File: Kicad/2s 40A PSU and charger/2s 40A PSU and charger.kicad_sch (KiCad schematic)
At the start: 0 parts

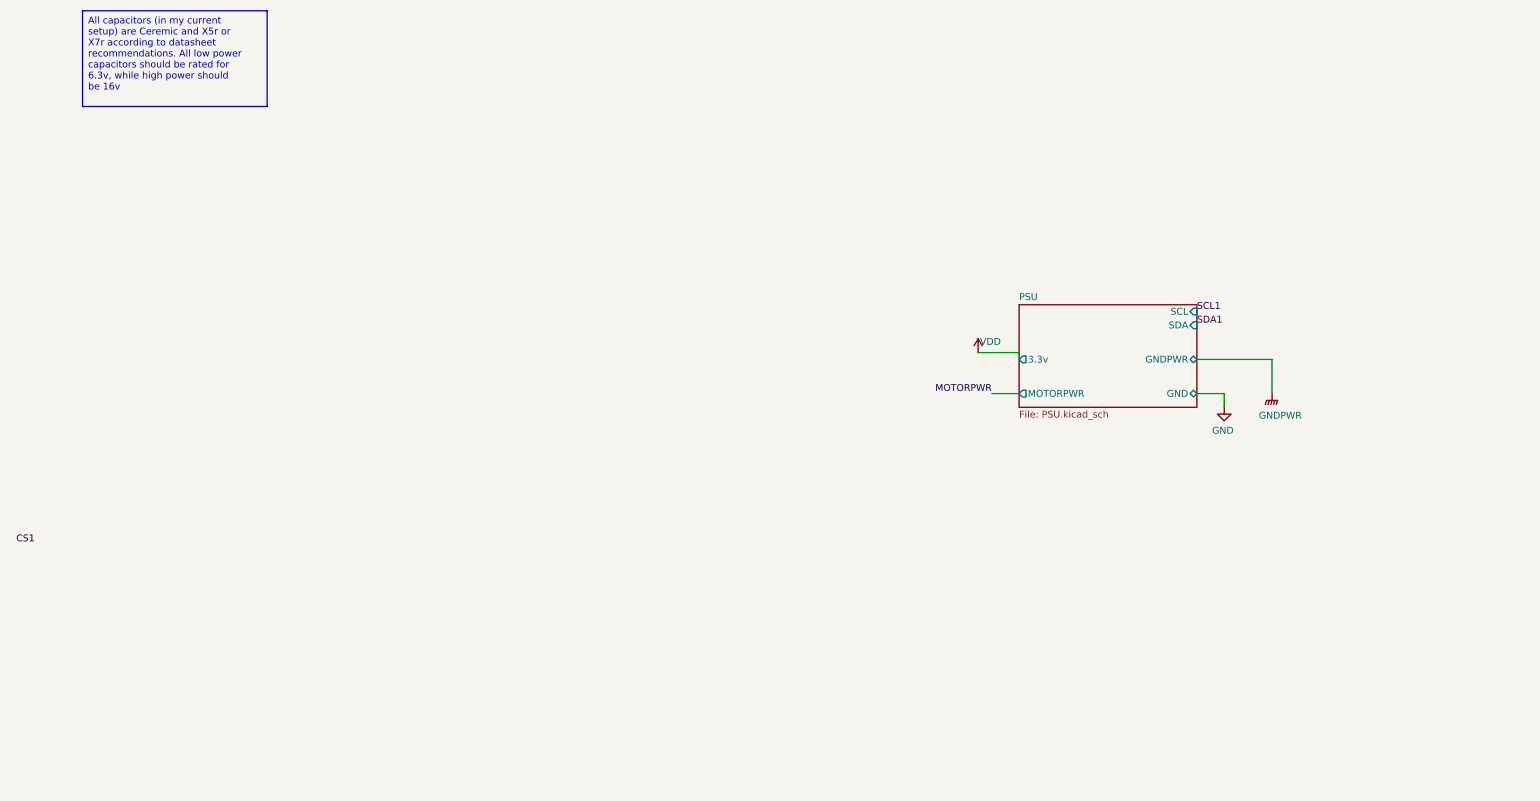
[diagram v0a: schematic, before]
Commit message: Rearranged schematic hierarchy
It should be clearer than the original design from my testing board. I haven't changed any of the design things except getting the correct small transistor footprint (errata from before)
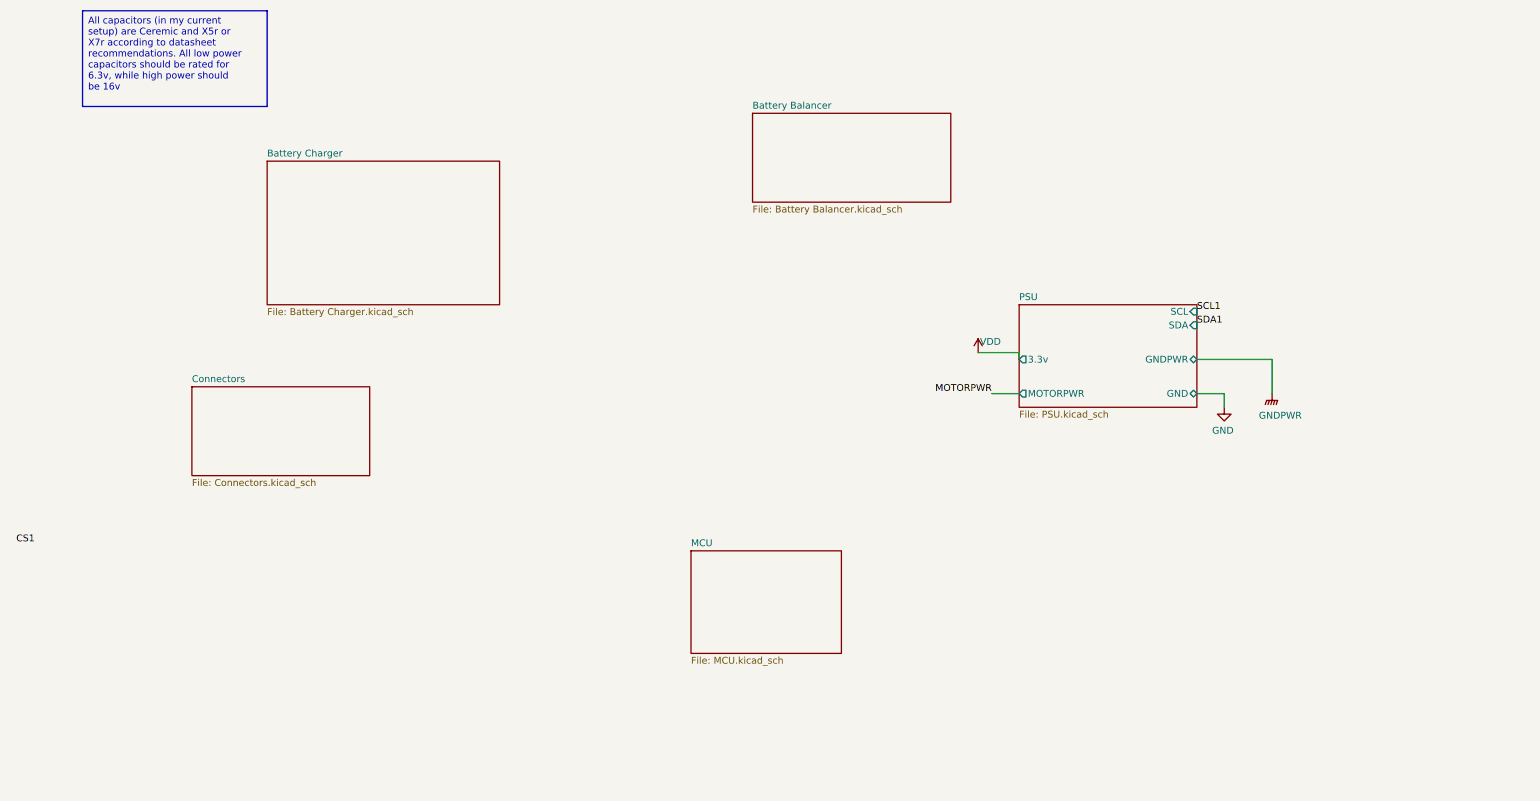
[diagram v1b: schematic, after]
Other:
- added sheet Battery Balancer (Battery Balancer.kicad_sch)
- added sheet Battery Charger (Battery Charger.kicad_sch)
- added sheet Connectors (Connectors.kicad_sch)
- added sheet MCU (MCU.kicad_sch)
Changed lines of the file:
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@@
+	)
+	(sheet
+		(at 40.64 83.82)
+		(size 33.02 16.51)
+		(fields_autoplaced yes)
+		(stroke
+			(width 0.1524)
+			(type solid)
+		)
+		(fill
+			(color 0 0 0 0.0000)
+		)
+		(property "Sheetname" "Connectors"
+			(at 40.64 83.1084 0)
+			(effects
+				(font
+					(size 1.27 1.27)
+				)
+				(justify left bottom)
+			)
+		)
+		(property "Sheetfile" "Connectors.kicad_sch"
+			(at 40.64 100.9146 0)
+			(effects
+				(font
+					(size 1.27 1.27)
+				)
+				(justify left top)
+			)
+		)
+		(instances
+			(project "2s 40A PSU and charger"
+				(path "/eb3f183d-8bb1-43a5-a363-092ed67891e3"
+					(page "5")
+				)
+			)
+		)
+	)
+	(sheet
+		(at 54.61 41.91)
+		(size 43.18 26.67)
+		(fields_autoplaced yes)
+		(stroke
+			(width 0.1524)
+			(type solid)
+		)
+		(fill
+			(color 0 0 0 0.0000)
+		)
+		(property "Sheetname" "Battery Charger"
+			(at 54.61 41.1984 0)
+			(effects
+				(font
+					(size 1.27 1.27)
+				)
+				(justify left bottom)
+			)
+		)
+		(property "Sheetfile" "Battery Charger.kicad_sch"
+			(at 54.61 69.1646 0)
+			(effects
+				(font
+					(size 1.27 1.27)
+				)
+				(justify left top)
+			)
+		)
+		(instances
+			(project "2s 40A PSU and charger"
+				(path "/eb3f183d-8bb1-43a5-a363-092ed67891e3"
+					(page "3")
+				)
+			)
+		)
+	)
+	(sheet
+		(at 133.35 114.3)
+		(size 27.94 19.05)
+		(fields_autoplaced yes)
+		(stroke
+			(width 0.1524)
+			(type solid)
+		)
+		(fill
+			(color 0 0 0 0.0000)
+		)
+		(property "Sheetname" "MCU"
+			(at 133.35 113.5884 0)
+			(effects
+				(font
+					(size 1.27 1.27)
+				)
+				(justify left bottom)
+			)
+		)
+		(property "Sheetfile" "MCU.kicad_sch"
+			(at 133.35 133.9346 0)
+			(effects
+				(font
+					(size 1.27 1.27)
+				)
+				(justify left top)
+			)
+		)
+		(instances
+			(project "2s 40A PSU and charger"
+				(path "/eb3f183d-8bb1-43a5-a363-092ed67891e3"
+					(page "6")
+				)
+			)
+		)
+	)
+	(sheet
+		(at 144.78 33.02)
+		(size 36.83 16.51)
+		(fields_autoplaced yes)
+		(stroke
+			(width 0.1524)
+			(type solid)
+		)
+		(fill
+			(color 0 0 0 0.0000)
+		)
+		(property "Sheetname" "Battery Balancer"
+			(at 144.78 32.3084 0)
+			(effects
+				(font
+					(size 1.27 1.27)
+				)
+				(justify left bottom)
+			)
+		)
+		(property "Sheetfile" "Battery Balancer.kicad_sch"
+			(at 144.78 50.1146 0)
+			(effects
+				(font
+					(size 1.27 1.27)
+				)
+				(justify left top)
+			)
+		)
+		(instances
+			(project "2s 40A PSU and charger"
+				(path "/eb3f183d-8bb1-43a5-a363-092ed67891e3"
+					(page "4")
+				)
+			)
+		)
 	)
 	(sheet

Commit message: Reworked PSU to use CH32X035 and USB-PD
This will save a few bucks and will actually be a cooler solution than just a DC jack connected to some pads
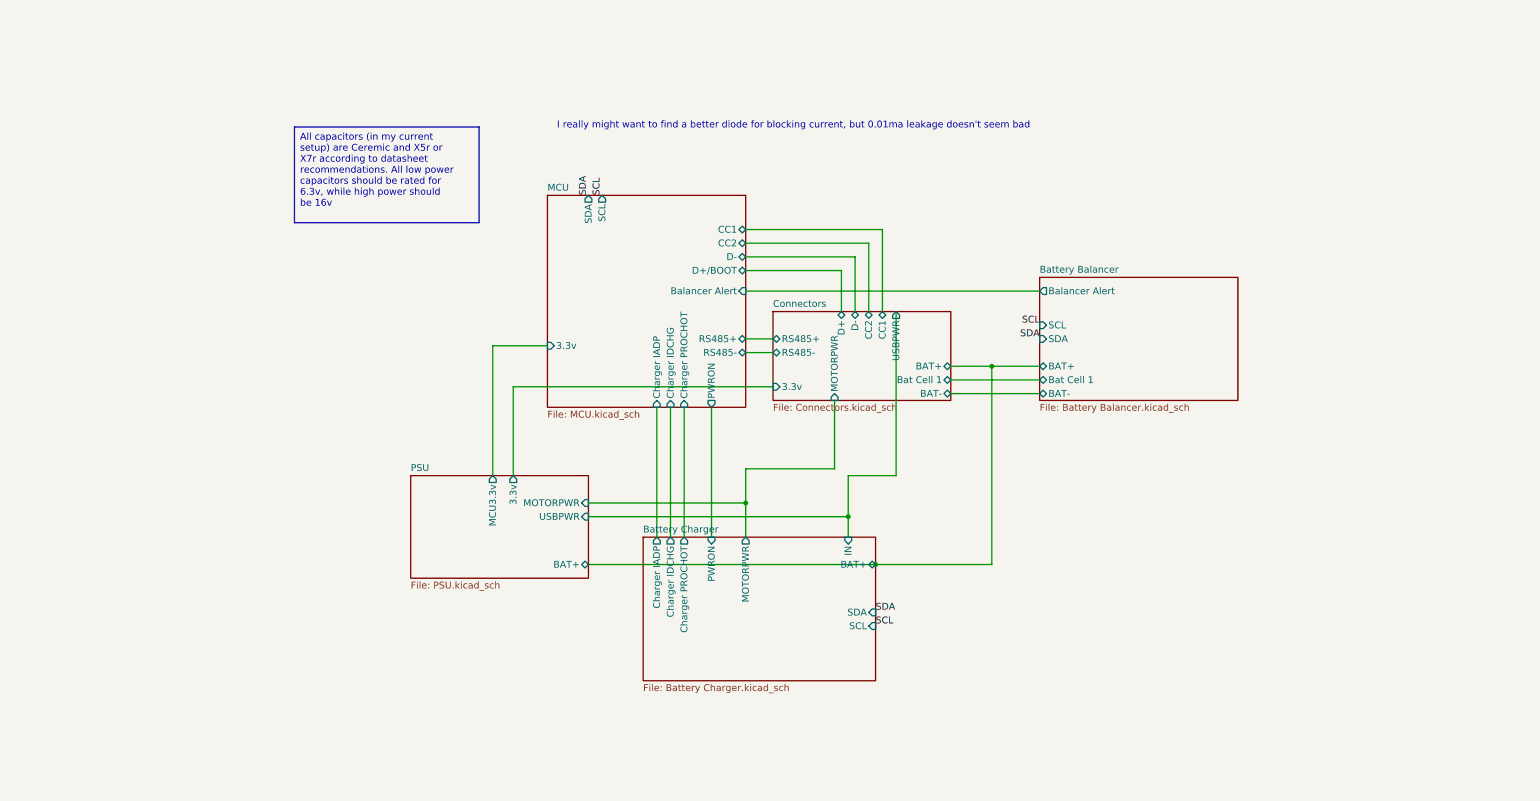
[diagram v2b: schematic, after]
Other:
- sheet Battery Balancer ports: added BAT+, BAT-, Balancer Alert, Bat Cell 1, SCL, SDA; removed none
- sheet Battery Charger ports: added BAT+, Charger IADP, Charger IDCHG, Charger PROCHOT, IN, MOTORPWR, PWRON, SCL, SDA; removed none
- sheet Connectors ports: added 3.3v, BAT+, BAT-, Bat Cell 1, CC1, CC2, D+, D-, MOTORPWR, RS485+, RS485-, USBPWR; removed none
- sheet MCU ports: added 3.3v, Balancer Alert, CC1, CC2, Charger IADP, Charger IDCHG, Charger PROCHOT, D+/BOOT, D-, PWRON, RS485+, RS485-, SCL, SDA; removed none
- sheet PSU ports: added BAT+, MCU3.3v, USBPWR; removed GND, GNDPWR, SCL, SDA
- note added: "I really might want to find a better diode for blocking current, but 0.01ma leakage doesn't seem bad"

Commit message: Improved schematic formatting and visuals
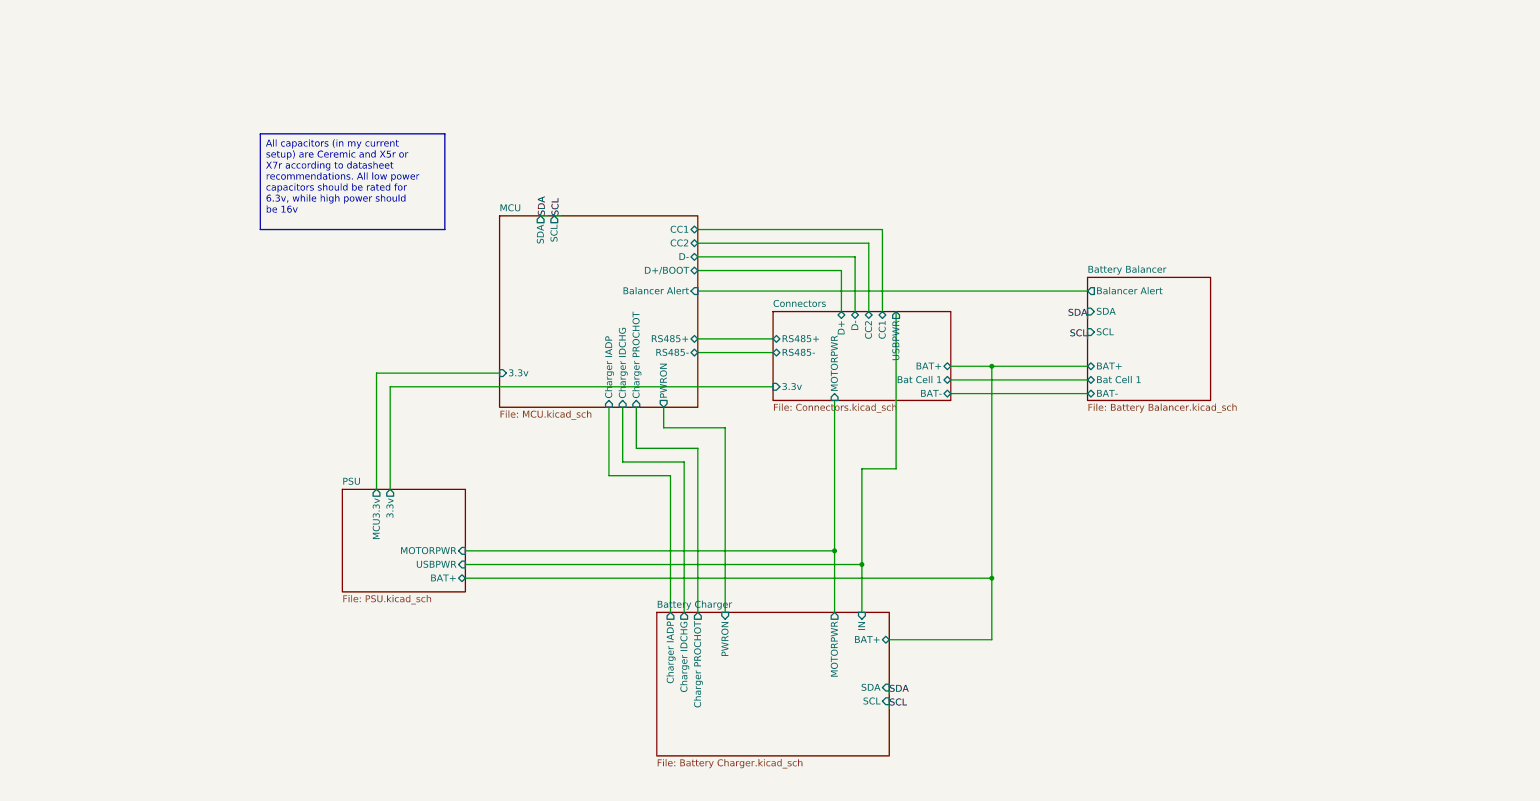
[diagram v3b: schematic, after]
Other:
- note removed: "I really might want to find a better diode for blocking current, but 0.01ma leakage doesn't seem bad"

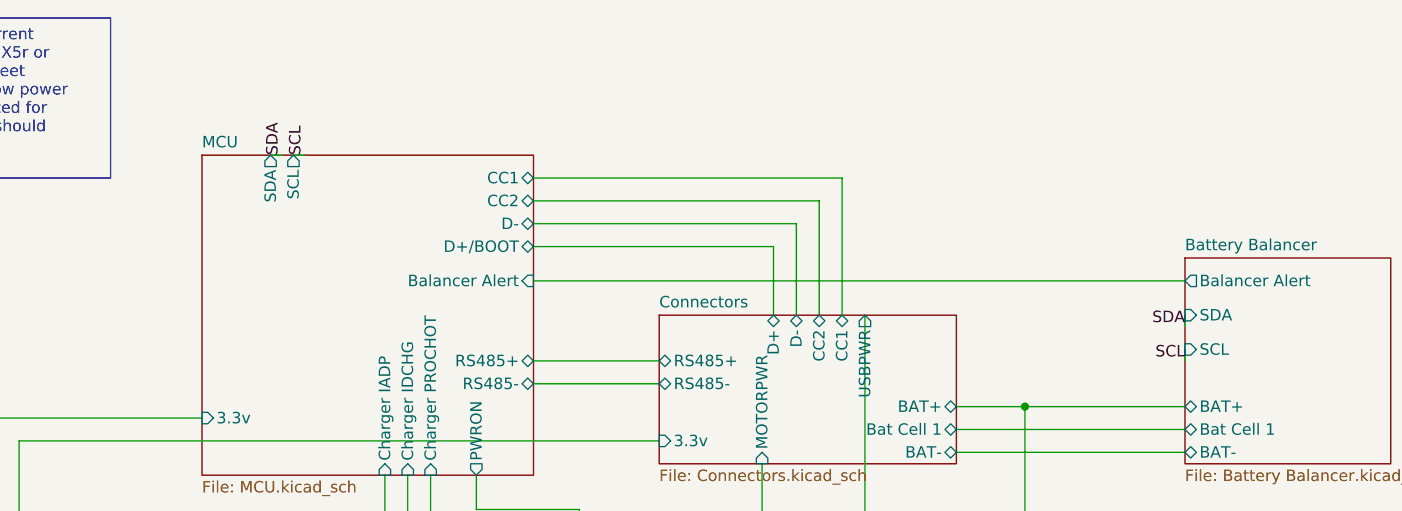
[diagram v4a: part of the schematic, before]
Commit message: Updated Ground connections and tweaked some formatting
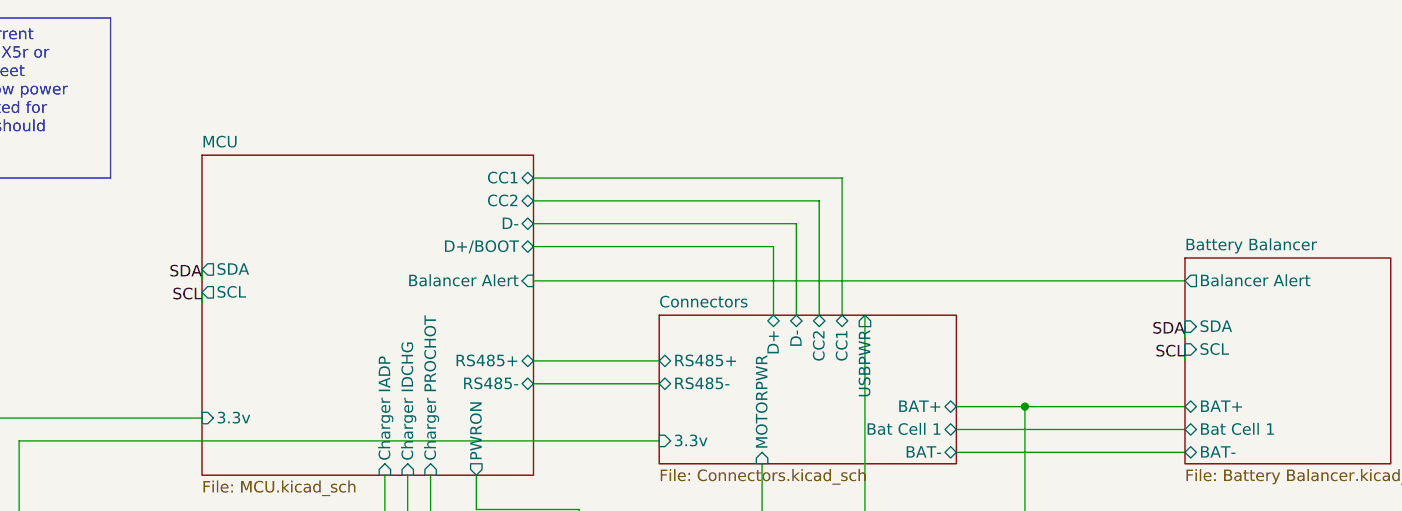
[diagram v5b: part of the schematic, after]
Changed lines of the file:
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@@
 	(wire
 		(pts
-			(xy 109.22 52.07) (xy 107.95 52.07)
+			(xy 97.79 68.58) (xy 97.79 67.31)
 		)
 		(stroke
@@
 	(wire
 		(pts
-			(xy 207.01 71.12) (xy 207.01 69.85)
-		)
-		(stroke
-			(width 0)
-			(type default)
-		)
-	)
-	(wire
-		(pts
 			(xy 181.61 82.55) (xy 207.01 82.55)
 		)
@@
 	(wire
 		(pts
+			(xy 207.01 72.39) (xy 207.01 71.12)
+		)
+		(stroke
+			(width 0)
+			(type default)
+		)
+	)
+	(wire
+		(pts
 			(xy 163.83 69.85) (xy 163.83 59.69)
 		)
@@
 	(wire
 		(pts
+			(xy 97.79 66.04) (xy 97.79 64.77)
+		)
+		(stroke
+			(width 0)
+			(type default)
+		)
+	)
+	(wire
+		(pts
 			(xy 134.62 95.25) (xy 134.62 125.73)
 		)
@@
 		(pts
 			(xy 189.23 80.01) (xy 207.01 80.01)
-		)
-		(stroke
-			(width 0)
-			(type default)
-		)
-	)
-	(wire
-		(pts
-			(xy 106.68 52.07) (xy 105.41 52.07)
 		)
 		(stroke
@@
 	)
 	(label "SDA"
-		(at 106.68 52.07 90)
+		(at 97.79 66.04 180)
 		(fields_autoplaced yes)
 		(effects
@@
 				(size 1.27 1.27)
 			)
-			(justify left bottom)
+			(justify right bottom)
 		)
 	)
@@
 	)
 	(label "SDA"
-		(at 207.01 71.12 180)
+		(at 207.01 72.39 180)
 		(fields_autoplaced yes)
 		(effects
@@
 	)
 	(label "SCL"
-		(at 109.22 52.07 90)
+		(at 97.79 68.58 180)
 		(fields_autoplaced yes)
 		(effects
@@
 				(size 1.27 1.27)
 			)
-			(justify left bottom)
+			(justify right bottom)
 		)
 	)
@@
 		)
 		(pin "SDA" output
-			(at 105.41 52.07 90)
-			(effects
-				(font
-					(size 1.27 1.27)
-				)
-				(justify right)
+			(at 97.79 64.77 180)
+			(effects
+				(font
+					(size 1.27 1.27)
+				)
+				(justify left)
 			)
 		)
 		(pin "SCL" output
-			(at 107.95 52.07 90)
-			(effects
-				(font
-					(size 1.27 1.27)
-				)
-				(justify right)
+			(at 97.79 67.31 180)
+			(effects
+				(font
+					(size 1.27 1.27)
+				)
+				(justify left)
 			)
 		)
@@
 		)
 		(pin "SDA" input
-			(at 207.01 69.85 180)
-			(effects
-				(font
+			(at 207.01 71.12 180)
+			(effects
+				(font
